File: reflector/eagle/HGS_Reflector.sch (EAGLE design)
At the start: 50 parts, among them J1 U.FL, J2 USB_MINI-B_SMT, J3 142-0701-851, J4 142-0701-851, T1 QWT2.4222, U1 LP2985XX-N, U2 LP2985XX-N, U3 NCS3-272+, U4 QPQ1907, U5 QPQ1907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

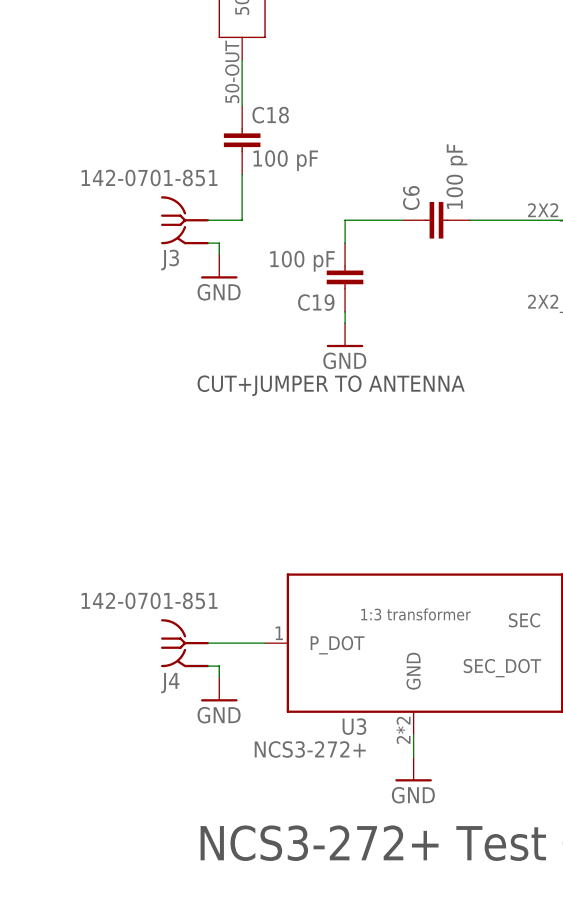
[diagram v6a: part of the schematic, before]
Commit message: Switched edge fired SMA connectors to Oliver's fancy SMT vertical connectors.
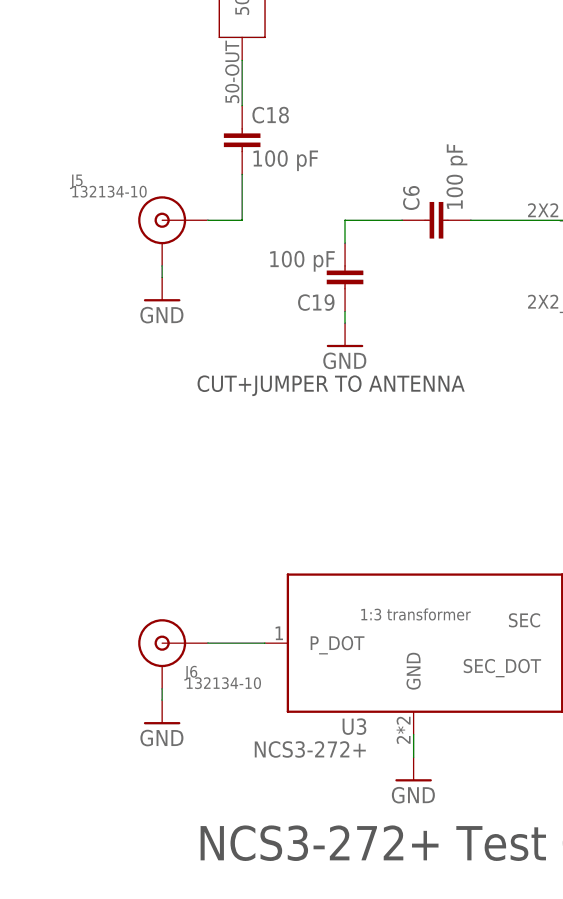
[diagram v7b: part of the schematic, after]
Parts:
- removed J3, J4: 142-0701-851, J-Cinch-142-0701-851-SMA-end-launch:142-0701-851
- added J5, J6: 132134-10, J-Amphenol-132134-10-SMA-F-SMT-vertical:132134-10
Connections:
- net GND: now also J5.GND, J6.GND; no longer J3.GND, J4.GND
- net N$23: now also J5.SIG; no longer J3.RF
- net N$24: now also J6.SIG; no longer J4.RF
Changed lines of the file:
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@@
 <part name="T1" library="TM-QWT-2.422GHz" deviceset="QWT2.422" device="2"/>
 <part name="C18" library="oresat-rcl" deviceset="C-EU" device="0402-C-NOSILK" value="100 pF"/>
-<part name="J3" library="J-Cinch-142-0701-851-SMA-end-launch" deviceset="142-0701-851" device=""/>
 <part name="GND10" library="supply1" library_urn="urn:adsk.eagle:library:371" deviceset="GND" device="">
 <attribute name="SPICEPREFIX" value="G"/>
 </part>
-<part name="J4" library="J-Cinch-142-0701-851-SMA-end-launch" deviceset="142-0701-851" device=""/>
 <part name="GND20" library="supply1" library_urn="urn:adsk.eagle:library:371" deviceset="GND" device="">
 <attribute name="SPICEPREFIX" value="G"/>
@@
 <part name="GND23" library="supply1" library_urn="urn:adsk.eagle:library:371" deviceset="GND" device=""/>
 <part name="E5" library="oresat-rcl" deviceset="L-BEAD-*" device="0603-B" value="BLM18GG471SZ1D"/>
+<part name="J5" library="J-Amphenol-132134-10-SMA-F-SMT-vertical" deviceset="132134-10" device=""/>
+<part name="J6" library="J-Amphenol-132134-10-SMA-F-SMT-vertical" deviceset="132134-10" device=""/>
 </parts>
 <sheets>
@@
 <attribute name="VALUE" x="31.496" y="82.169" size="1.778" layer="96"/>
 </instance>
-<instance part="J3" gate="G$1" x="24.13" y="76.2" smashed="yes">
-<attribute name="NAME" x="21.59" y="71.12" size="1.778" layer="95"/>
-<attribute name="VALUE" x="27.94" y="80.01" size="1.778" layer="96" rot="MR0"/>
-</instance>
-<instance part="GND10" gate="1" x="27.94" y="69.85" smashed="yes">
-<attribute name="VALUE" x="25.4" y="67.31" size="1.778" layer="96"/>
-</instance>
-<instance part="J4" gate="G$1" x="24.13" y="29.21" smashed="yes">
-<attribute name="NAME" x="21.59" y="24.13" size="1.778" layer="95"/>
-<attribute name="VALUE" x="27.94" y="33.02" size="1.778" layer="96" rot="MR0"/>
-</instance>
-<instance part="GND20" gate="1" x="27.94" y="22.86" smashed="yes">
-<attribute name="VALUE" x="25.4" y="20.32" size="1.778" layer="96"/>
+<instance part="GND10" gate="1" x="21.59" y="67.31" smashed="yes">
+<attribute name="VALUE" x="19.05" y="64.77" size="1.778" layer="96"/>
+</instance>
+<instance part="GND20" gate="1" x="21.59" y="20.32" smashed="yes">
+<attribute name="VALUE" x="19.05" y="17.78" size="1.778" layer="96"/>
 </instance>
 <instance part="U3" gate="G$1" x="49.53" y="29.21" smashed="yes" rot="MR0">
@@
 <attribute name="NAME" x="214.122" y="156.21" size="1.778" layer="95"/>
 <attribute name="VALUE" x="203.962" y="149.606" size="1.778" layer="96"/>
+</instance>
+<instance part="J5" gate="G$1" x="21.59" y="76.2" smashed="yes">
+<attribute name="NAME" x="11.43" y="80.01" size="1.270859375" layer="95"/>
+<attribute name="VALUE" x="11.43" y="78.74" size="1.2703" layer="96"/>
+</instance>
+<instance part="J6" gate="G$1" x="21.59" y="29.21" smashed="yes">
+<attribute name="NAME" x="24.13" y="25.4" size="1.270859375" layer="95"/>
+<attribute name="VALUE" x="24.13" y="24.13" size="1.2703" layer="96"/>
 </instance>
 </instances>
@@
 </segment>
 <segment>
-<pinref part="J3" gate="G$1" pin="GND"/>
-<wire x1="26.67" y1="73.66" x2="27.94" y2="73.66" width="0.1524" layer="91"/>
-<pinref part="GND10" gate="1" pin="GND"/>
-<wire x1="27.94" y1="73.66" x2="27.94" y2="72.39" width="0.1524" layer="91"/>
-</segment>
-<segment>
-<pinref part="J4" gate="G$1" pin="GND"/>
-<wire x1="26.67" y1="26.67" x2="27.94" y2="26.67" width="0.1524" layer="91"/>
-<pinref part="GND20" gate="1" pin="GND"/>
-<wire x1="27.94" y1="26.67" x2="27.94" y2="25.4" width="0.1524" layer="91"/>
-</segment>
-<segment>
 <pinref part="U3" gate="G$1" pin="GND"/>
 <pinref part="GND21" gate="1" pin="GND"/>
@@
 <pinref part="GND23" gate="1" pin="GND"/>
 <wire x1="231.14" y1="144.78" x2="231.14" y2="147.32" width="0.1524" layer="91"/>
+</segment>
+<segment>
+<pinref part="J5" gate="G$1" pin="GND"/>
+<pinref part="GND10" gate="1" pin="GND"/>
+<wire x1="21.59" y1="69.85" x2="21.59" y2="71.12" width="0.1524" layer="91"/>
+</segment>
+<segment>
+<pinref part="J6" gate="G$1" pin="GND"/>
+<pinref part="GND20" gate="1" pin="GND"/>
+<wire x1="21.59" y1="22.86" x2="21.59" y2="24.13" width="0.1524" layer="91"/>
 </segment>
 </net>
@@
 <net name="N$23" class="2">
 <segment>
-<pinref part="J3" gate="G$1" pin="RF"/>
 <pinref part="C18" gate="CE" pin="2"/>
 <wire x1="26.67" y1="76.2" x2="30.48" y2="76.2" width="0.1524" layer="91"/>
 <wire x1="30.48" y1="76.2" x2="30.48" y2="81.28" width="0.1524" layer="91"/>
+<pinref part="J5" gate="G$1" pin="SIG"/>
 </segment>
 </net>
 <net name="N$24" class="2">
 <segment>
-<pinref part="J4" gate="G$1" pin="RF"/>
 <pinref part="U3" gate="G$1" pin="P_DOT"/>
 <wire x1="26.67" y1="29.21" x2="33.02" y2="29.21" width="0.1524" layer="91"/>
-</segment>
-</net>
+<pinref part="J6" gate="G$1" pin="SIG"/>
+</segment>
+</net>

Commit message: Added more stitching to RF connectors, and added possible connection to the WF Atheros card... might work? Might not? First round try!
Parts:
- removed U$4: AR9721WF, AR9721:AR9721WF
- added C21: 100 pF, oresat-rcl:C-EU0603-C-NOSILK
- added J3: SM06B-SRSS-TB(LF)(SN), J-JST-SM06B-SRSS-TB(LF)(SN)-1mm-smt-6pin:SM06B-SRSS-TB(LF)(SN)
- added LED2: GREEN, SparkFun-LED:LED-GREEN0603
- added PCBA1: WF-NP9202WF, PCBA-WF-NP9202-wifi-adapter:WF-NP9202WF
- added R6: 0, oresat-rcl:R-US_0603-B-NOSILK
- added R7: 1k, oresat-rcl:R-US_0603-B-NOSILK
- added TP2: TEST-POINT-LARGE-SQUARE, oresat-misc:TEST-POINT-LARGE-SQUARE
- added X1: (no value), BeagleBone_Blue_R3:USB_HOST_W/CHASSIS_GND
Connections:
- new net N$31: J3.6, R6.2
- new net N$32: LED2.A, R7.1
- new net N$33: J3.2, X1.D+
- new net N$34: J3.5, LED2.C
- new net N$36: J3.3, X1.D-
- new net N$37: TP2.1, X1.VBUS
- new net N$38: C21.2, X1.CG1, X1.CG2
- net GND: now also C21.1, J3.4, J3.7, X1.GND
- net N$29: now also J3.1, R6.1, R7.2
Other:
- note added: "!LED"
- note added: "6" MicroUSB to Type A Connector"
- note added: "D+"
- note added: "D-"
- note added: "GND"
- note added: "JST A06SR06SR30K51A 2x 6pin 1mm cable assembly"
- note added: "ON/!OFF"
- note added: "VUSB"
- moved on the sheet: C1, C10, C11, C12, C13, C14, C15, C16, C17, C18, C19, C2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
